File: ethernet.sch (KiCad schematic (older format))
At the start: 55 parts, among them IC2 TLV73312PDBVT, J1 L834-1G1T-S7, U20 KSZ9031RNXCA, Y2 ABM8G-25.000MHZ-18-D2Y-T

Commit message: Updated local libs
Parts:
- C196, C198, C199, C200, C206: footprint antmicro-footprints:0402-cap -> artix-dc-scm-footprints:0402-cap; symbol antmicroCapacitors0402:C_4u7_0402 -> artix-dc-scm:C_4u7_0402
- C197, C201, C202, C204, C205: footprint antmicro-footprints:0402-cap -> artix-dc-scm-footprints:0402-cap; symbol antmicroCapacitors0402:C_470n_0402 -> artix-dc-scm:C_470n_0402
- C2, C3: footprint antmicro-footprints:0402-cap -> artix-dc-scm-footprints:0402-cap; symbol antmicroCapacitors0402:C_1u_0402 -> artix-dc-scm:C_1u_0402
- C203, C225, C226, C227, C228: footprint antmicro-footprints:0402-cap -> artix-dc-scm-footprints:0402-cap; symbol antmicroCapacitors0402:C_100n_0402 -> artix-dc-scm:C_100n_0402
- C207, C208, C209, C210, C211, C212, C213, C214, C215, C216, C217, C218, C219: footprint antmicro-footprints:0402-cap -> artix-dc-scm-footprints:0402-cap; symbol antmicroCapacitors0402:C_10n_0402 -> artix-dc-scm:C_10n_0402
- C220, C221: footprint antmicro-footprints:0402-cap -> artix-dc-scm-footprints:0402-cap; symbol antmicroCapacitors0402:C_22p_0402 -> artix-dc-scm:C_22p_0402
- FB4, FB5, FB6: footprint antmicro-footprints:0603-res -> artix-dc-scm-footprints:0603-res; symbol antmicroFerriteBeadsandChips:BLM18PG121SN1D -> artix-dc-scm:BLM18PG121SN1D
- IC2: footprint antmicro-footprints:SOT-23-5 -> artix-dc-scm-footprints:SOT-23-5; symbol antmicroPMICVoltageRegulatorsLinear:TLV73312PDBVT -> artix-dc-scm:TLV73312PDBVT
- J1: footprint antmicro-footprints:BEL_L834-1G1T-S7 -> artix-dc-scm-footprints:BEL_L834-1G1T-S7; symbol antmicroModularConnectorsJacksWithMagnetics:L834-1G1T-S7 -> artix-dc-scm:L834-1G1T-S7
- R127, R148, R149, R150, R151, R152, R153, R154, R155, R156, R157, R158: footprint antmicro-footprints:0402-res -> artix-dc-scm-footprints:0402-res; symbol antmicroResistors0402:R_10k2_0402 -> artix-dc-scm:R_10k2_0402
- R159: footprint antmicro-footprints:0402-res -> artix-dc-scm-footprints:0402-res; symbol antmicroResistors0402:R_12k1_0402 -> artix-dc-scm:R_12k1_0402
- R160: footprint antmicro-footprints:0402-res -> artix-dc-scm-footprints:0402-res; symbol antmicroResistors0402:R_1M8_0402 -> artix-dc-scm:R_1M8_0402
- U20: footprint antmicro-footprints:QFN-48-Microchip-QFN77-48LD-PL-2 -> artix-dc-scm-footprints:QFN-48-Microchip-QFN77-48LD-PL-2; symbol antmicroInterfaceControllers:KSZ9031RNXCA -> artix-dc-scm:KSZ9031RNXCA
- Y2: footprint antmicro-footprints:KX-7 -> artix-dc-scm-footprints:KX-7; symbol antmicroCrystals:ABM8G-25.000MHZ-18-D2Y-T -> artix-dc-scm:ABM8G-25.000MHZ-18-D2Y-T

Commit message: Replaced 1V2 voltage regulator
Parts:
- removed C2, C3: C_1u_0402, artix-dc-scm-footprints:0402-cap, symbol artix-dc-scm:C_1u_0402
- removed IC2: TLV73312PDBVT, artix-dc-scm-footprints:SOT-23-5, symbol artix-dc-scm:TLV73312PDBVT
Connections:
- wire segments 254 -> 246
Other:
- note removed: "1V2 LDO"
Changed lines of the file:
@@
 Text Notes 1800 8250 0    118  ~ 24
 AVDDL decoupling
-$Comp
-L artix-dc-scm:TLV73312PDBVT IC2
-U 1 1 616A1A6B
-P 6450 9925
-F 0 "IC2" H 6450 10406 50  0000 C CNN
-F 1 "TLV73312PDBVT" H 6450 10323 39  0000 C CNN
-F 2 "artix-dc-scm-footprints:SOT-23-5" H 6450 9675 50  0001 C CNN
-F 3 "" H 6550 10275 50  0001 C CNN
-F 4 "TLV73312PDBVT" H 6450 10240 50  0000 C CNN "MPN"
-F 5 "Texas Instruments" H 6450 10149 50  0000 C CNN "Manufacturer"
-	1    6450 9925
-	1    0    0    -1
-$EndComp
-Text Notes 6125 8825 0    118  ~ 24
-1V2 LDO
-Wire Wire Line
-	6050 9975 6050 9875
-Connection ~ 6050 9875
-Wire Wire Line
-	6050 9875 6050 9500
-Wire Wire Line
-	6850 9875 6850 9500
-Wire Wire Line
-	6850 9975 6850 10225
-$Comp
-L artix-dc-scm:GND #PWR?
-U 1 1 6171C0C6
-P 6850 10225
-AR Path="/5FF245C4/6171C0C6" Ref="#PWR?"  Part="1"
-AR Path="/60570C04/6171C0C6" Ref="#PWR05"  Part="1"
-F 0 "#PWR05" H 6850 9975 50  0001 C CNN
-F 1 "GND" H 6855 10052 50  0000 C CNN
-F 2 "" H 6850 10225 50  0001 C CNN
-F 3 "" H 6850 10225 50  0001 C CNN
-	1    6850 10225
-	1    0    0    -1
-$EndComp
-Text GLabel 6850 9500 1    50   Input ~ 0
-VCC1V2
-Text GLabel 6050 9500 1    50   Input ~ 0
-VCC3V3
-Text GLabel 5775 9500 1    50   Input ~ 0
-VCC3V3
-Text GLabel 7075 9500 1    50   Input ~ 0
-VCC1V2
-Wire Wire Line
-	7075 9500 7075 9625
-Wire Wire Line
-	5775 9500 5775 9625
-$Comp
-L artix-dc-scm:GND #PWR?
-U 1 1 6175ECB0
-P 5775 10100
-AR Path="/5FF245C4/6175ECB0" Ref="#PWR?"  Part="1"
-AR Path="/60570C04/6175ECB0" Ref="#PWR04"  Part="1"
-F 0 "#PWR04" H 5775 9850 50  0001 C CNN
-F 1 "GND" H 5780 9927 50  0000 C CNN
-F 2 "" H 5775 10100 50  0001 C CNN
-F 3 "" H 5775 10100 50  0001 C CNN
-	1    5775 10100
-	1    0    0    -1
-$EndComp
-Wire Wire Line
-	5775 9925 5775 10100
-$Comp
-L artix-dc-scm:GND #PWR?
-U 1 1 61786A7C
-P 7075 10100
-AR Path="/5FF245C4/61786A7C" Ref="#PWR?"  Part="1"
-AR Path="/60570C04/61786A7C" Ref="#PWR06"  Part="1"
-F 0 "#PWR06" H 7075 9850 50  0001 C CNN
-F 1 "GND" H 7080 9927 50  0000 C CNN
-F 2 "" H 7075 10100 50  0001 C CNN
-F 3 "" H 7075 10100 50  0001 C CNN
-	1    7075 10100
-	1    0    0    -1
-$EndComp
-Wire Wire Line
-	7075 9925 7075 10100
-$Comp
-L artix-dc-scm:C_1u_0402 C2
-U 1 1 6179EAA3
-P 5775 9775
-F 0 "C2" H 5890 9820 60  0000 L CNN
-F 1 "C_1u_0402" H 5775 9625 60  0001 C CNN
-F 2 "artix-dc-scm-footprints:0402-cap" H 5975 9975 60  0001 L CNN
-F 3 "" H 5775 9775 50  0001 C CNN
-F 4 "TDK" H 5975 10175 60  0001 L CNN "Manufacturer"
-F 5 "C1005X6S1A105K050BC" H 5975 10075 60  0001 L CNN "MPN"
-F 6 "1u" H 5890 9722 50  0000 L CNN "Val"
-	1    5775 9775
-	1    0    0    -1
-$EndComp
-$Comp
-L artix-dc-scm:C_1u_0402 C3
-U 1 1 6179F132
-P 7075 9775
-F 0 "C3" H 7190 9820 60  0000 L CNN
-F 1 "C_1u_0402" H 7075 9625 60  0001 C CNN
-F 2 "artix-dc-scm-footprints:0402-cap" H 7275 9975 60  0001 L CNN
-F 3 "" H 7075 9775 50  0001 C CNN
-F 4 "TDK" H 7275 10175 60  0001 L CNN "Manufacturer"
-F 5 "C1005X6S1A105K050BC" H 7275 10075 60  0001 L CNN "MPN"
-F 6 "1u" H 7190 9722 50  0000 L CNN "Val"
-	1    7075 9775
-	1    0    0    -1
-$EndComp
 Text Label 8400 3375 0    50   ~ 0
 DVDDL

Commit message: Cleaned up schematics
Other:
- moved on the sheet: C196, C197, C198, C199, C200, C201, C202, C203, C204, C205, C206, C207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

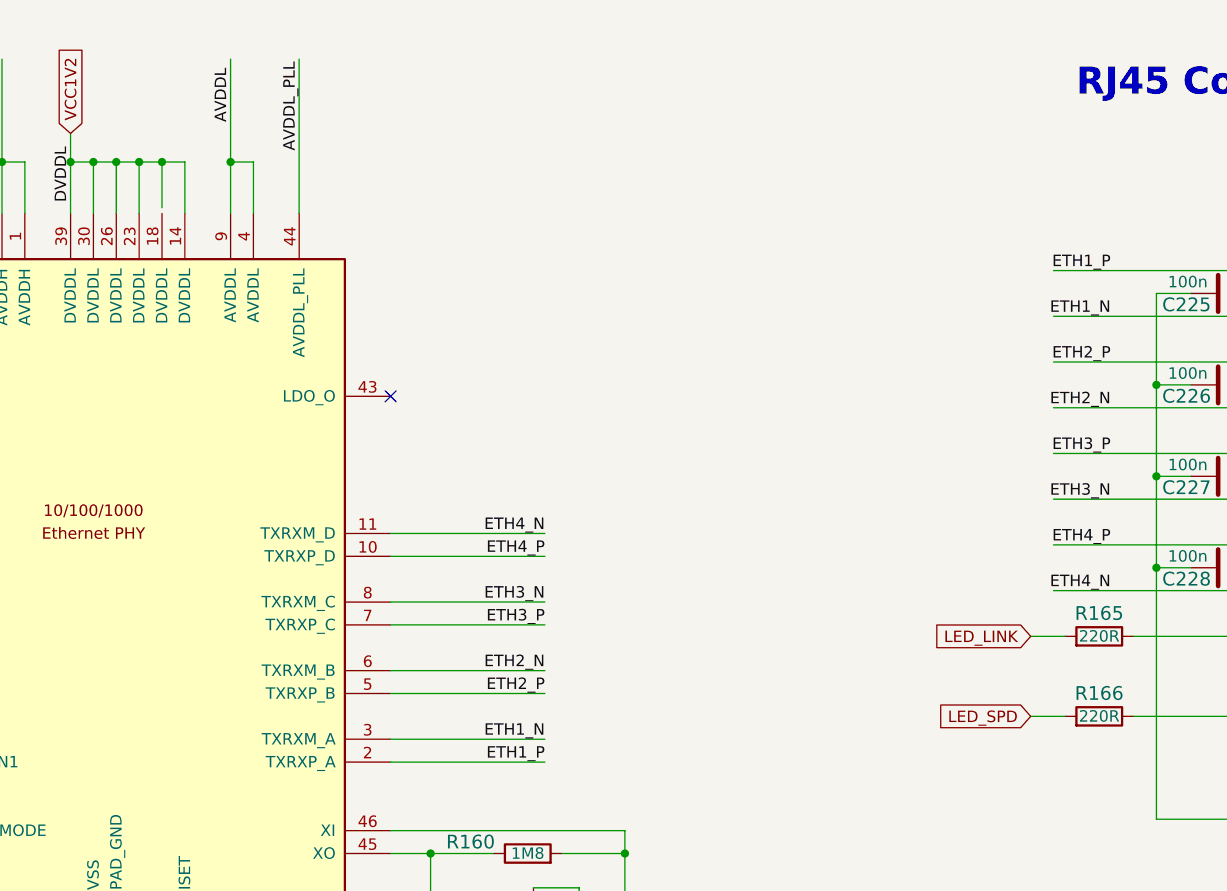
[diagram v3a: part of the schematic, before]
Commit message: Fix unconected DVDDL pin and ETH LED labels
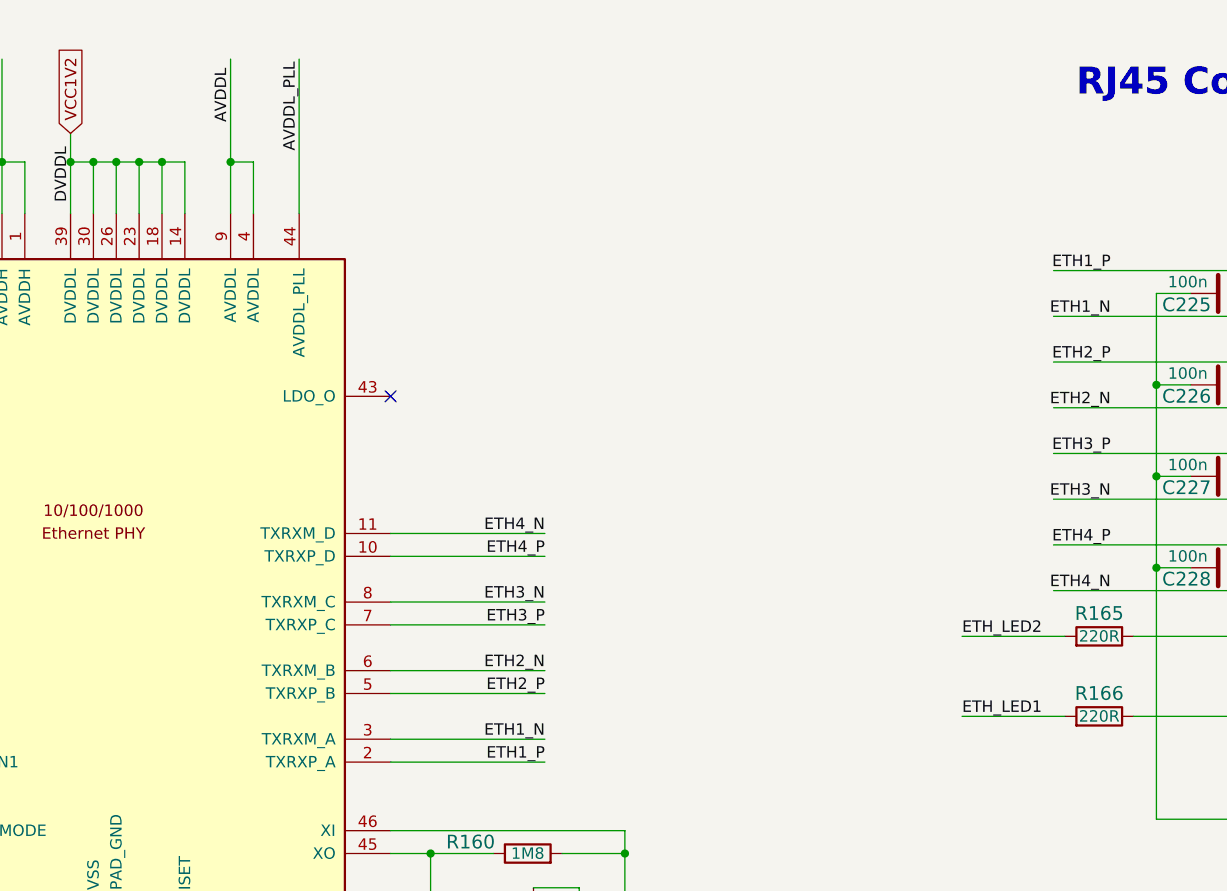
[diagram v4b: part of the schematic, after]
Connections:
- net labels removed: LED_LINK, LED_SPD
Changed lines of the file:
@@
 Comment4 ""
 $EndDescr
-Text GLabel 12300 5800 0    50   Input ~ 0
-LED_SPD
 Text Notes 13900 3100 2    118  ~ 24
 RJ45 Connector
@@
 	8400 3375 8300 3375
 Wire Wire Line
-	8500 3575 8500 3375
+	8500 3600 8500 3375
 Connection ~ 8500 3375
 Wire Wire Line
@@
 $EndComp
 Wire Wire Line
-	12300 5450 12450 5450
-Text GLabel 12300 5450 0    50   Input ~ 0
-LED_LINK
-Wire Wire Line
-	12300 5800 12450 5800
+	12000 5450 12450 5450
+Wire Wire Line
+	12000 5800 12450 5800
 Wire Wire Line
 	13300 5550 13250 5550
@@
 Wire Wire Line
 	12850 4350 12850 4750
+Text Label 12000 5800 0    50   ~ 0
+ETH_LED1
+Text Label 12000 5450 0    50   ~ 0
+ETH_LED2
 $EndSCHEMATC
